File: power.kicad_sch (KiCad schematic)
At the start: 6 parts, among them U2 NCV4274AST33T3G

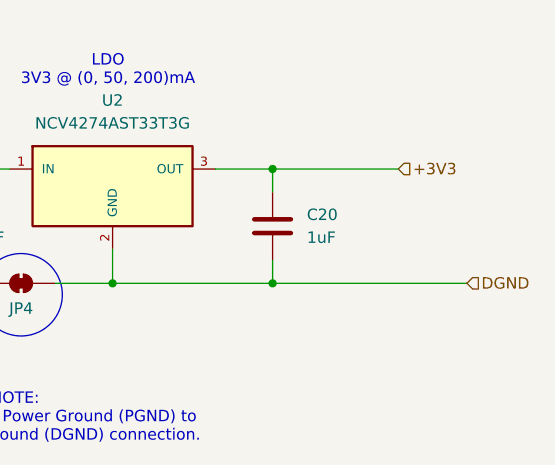
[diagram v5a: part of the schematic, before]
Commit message: Added part-numbers and updated symbols
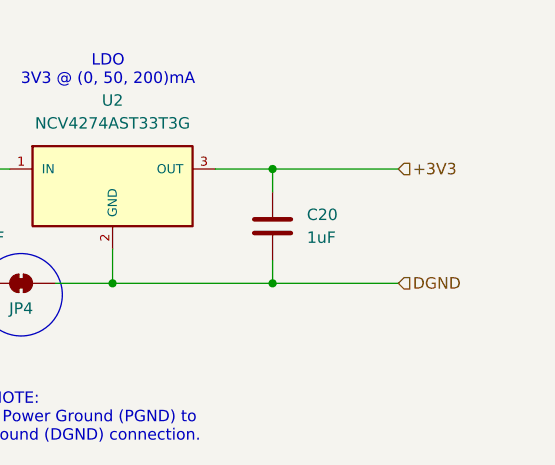
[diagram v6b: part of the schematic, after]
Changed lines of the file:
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@@
 	(wire
 		(pts
-			(xy 209.55 99.06) (xy 231.14 99.06)
+			(xy 209.55 99.06) (xy 223.52 99.06)
 		)
 		(stroke
@@
 	(hierarchical_label "DGND"
 		(shape input)
-		(at 231.14 99.06 0)
+		(at 223.52 99.06 0)
 		(effects
 			(font

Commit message: Layout Draft Complete
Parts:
- removed U2: NCV4274AST33T3G, KSE_DCDC:SOT230P700X175-4N, symbol KSE_DCDC:NCV4274AST33T3G
- added U2: AP7375-33SA-7, KSE_DCDC:AP7375-33SA-7_DIO, symbol KSE_DCDC:AP7375-33SA-7
- C1, C20: footprint Capacitor_SMD:C_1206_3216Metric -> Capacitor_SMD:C_0402_1005Metric
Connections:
- net +3V3: now also U2.2 (VOUT)
- net at C1.1, D1.1 (K), D3.1 (K): now also U2.1 (VIN)
- net 10–26V to 9V2A Step-Down Converter/+9V renamed +9V
- net GND renamed DGND
- net DGND: now also U2.3 (GND)
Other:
- moved on the sheet: C20, JP4

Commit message: Finished DRC/ERC
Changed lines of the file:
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@@
 		)
 	)
-	(hierarchical_label "VBAT"
+	(hierarchical_label "V_BAT"
 		(shape input)
 		(at 63.5 66.04 180)
@@
 			)
 		)
-		(property "Datasheet" "https://www.vishay.com/docs/88746/ss12.pdf"
+		(property "Datasheet" "~"
 			(at 160.02 88.9 0)
 			(effects
@@
 	)
 	(symbol
+		(lib_name "D_Schottky_1")
 		(lib_id "KSE_Diodes:D_Schottky")
 		(at 160.02 83.82 180)
@@
 			)
 		)
-		(property "Datasheet" "https://www.vishay.com/docs/88746/ss12.pdf"
+		(property "Datasheet" "~"
 			(at 160.02 83.82 0)
 			(effects
